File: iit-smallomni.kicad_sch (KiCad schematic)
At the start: 88 parts, among them J1 Battery, J10 DC-Motor, J11 Conn_02x05_Odd_Even, J12 LiPo guard, J2 HC_SR04, J3 HC_SR04, J4 HC_SR04, J5 DC-Motor, J6 DC-Motor, J7 DC-Motor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

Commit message: JTAG signal naming fixed
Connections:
- net JTAG_TCK renamed Mot3_DrvA-JTAG_TCK
- net JTAG_TDI renamed Mot2_DrvB-JTAG_TDI
- net JTAG_TDO renamed Mot1_DrvA-JTAG_TDO
- net JTAG_TMS renamed Mot2_DrvA-JTAG_TMS
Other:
- note added: "Battery measurement interface"
- note added: "JTAG interface"
- note added: "Mounting holes"
- company: (none) -> BME Irányítástechnika és Informatika Tanszék
- moved on the sheet: D10, D5, D6, D7, D8, D9, H1, H2, H3, H4, J11, J12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

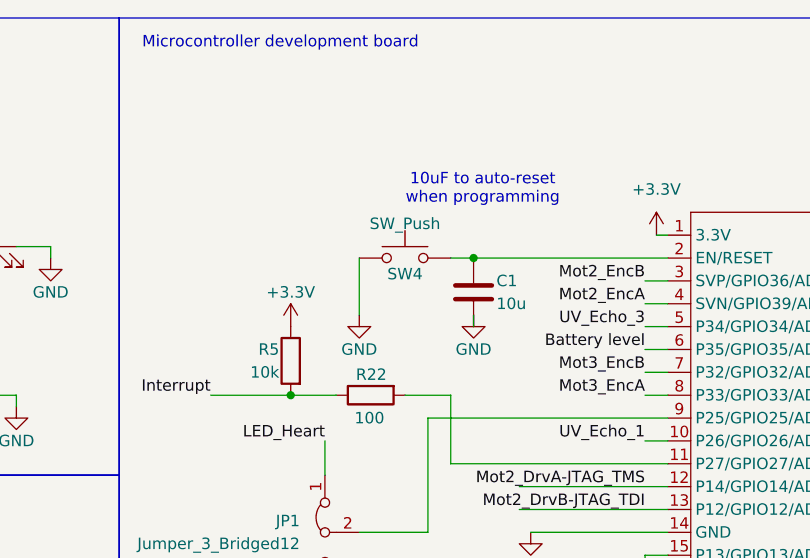
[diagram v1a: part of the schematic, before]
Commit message: Tidy up silkscreen, eliminate warnings
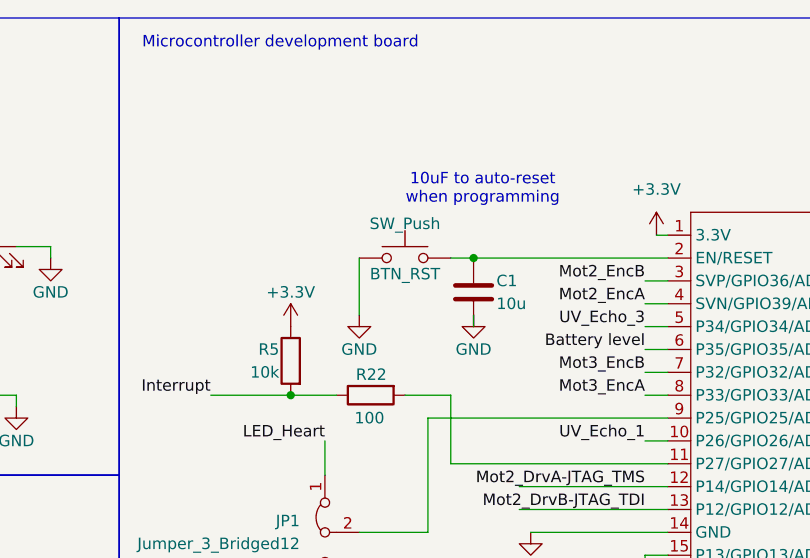
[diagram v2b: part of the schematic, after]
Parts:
- renumbered SW4 to BTN_RST
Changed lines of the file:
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@@
 		(on_board yes)
 		(dnp no)
-		(property "Reference" "SW4"
+		(property "Reference" "BTN_RST"
 			(at 163.83 41.148 0)
 			(effects
@@
 			(project "iit-smallomni"
 				(path "/7bce4676-45a5-4a88-afc4-c22791068c92"
-					(reference "SW4")
+					(reference "BTN_RST")
 					(unit 1)
 				)

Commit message: Update schematic export
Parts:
- renumbered BTN_RST to BTN_RST1
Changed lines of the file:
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@@
 		(on_board yes)
 		(dnp no)
-		(property "Reference" "BTN_RST"
+		(property "Reference" "BTN_RST1"
 			(at 163.83 41.148 0)
 			(effects
@@
 			(project "iit-smallomni"
 				(path "/7bce4676-45a5-4a88-afc4-c22791068c92"
-					(reference "BTN_RST")
+					(reference "BTN_RST1")
 					(unit 1)
 				)
